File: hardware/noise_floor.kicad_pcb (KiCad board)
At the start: 2 copper layers, 51.5 x 61.6 mm, 13 parts, among them J1 Input, J2 Output, J3 DC Power, J4 IO/Effect Connector 1 (IO Sid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, J5 IO/Switch Connector 1 (IO Sid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, J6 IO/Switch Connector 2 (IO Sid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, J7 IO/Switch Connector 1 (Switch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, J8 IO/Switch Connector 2 (Switch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, SW1 Footswitch

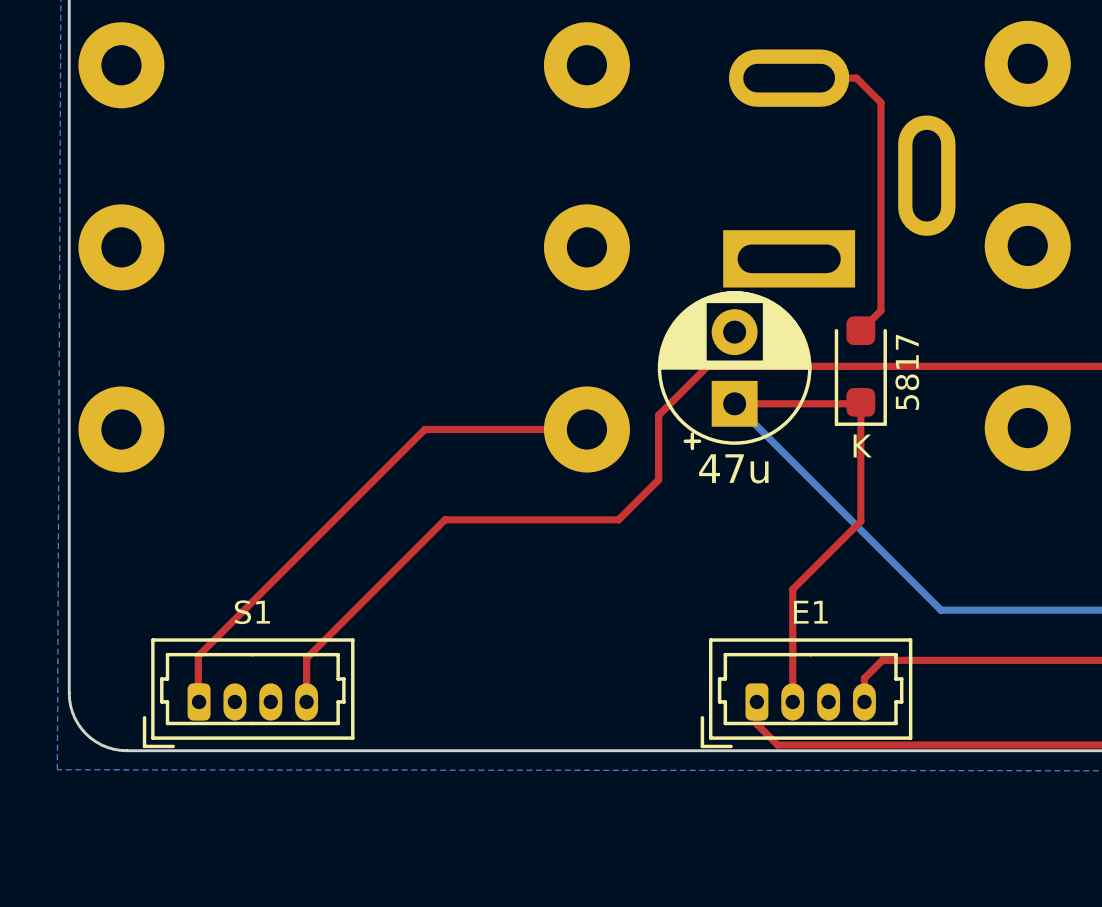
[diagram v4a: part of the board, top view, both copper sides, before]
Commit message: v0.05, added switched power input and optional battery connection
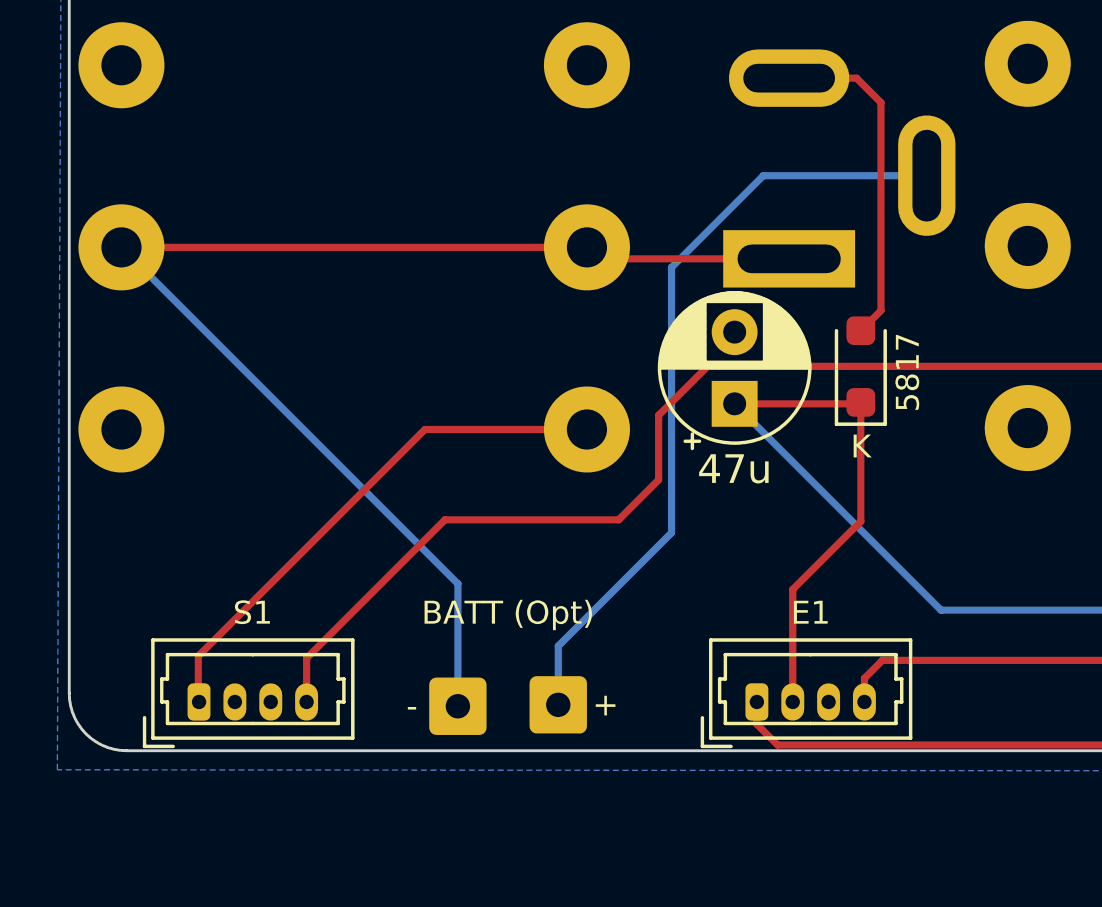
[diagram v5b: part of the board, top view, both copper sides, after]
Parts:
- added J4: Battery Negative (optional), Connector_Wire:SolderWire-0.25sqmm_1x01_D0.65mm_OD2mm, F.Cu at (29.1, 46.0)
- added J5: Battery Positive (optional), Connector_Wire:SolderWire-0.25sqmm_1x01_D0.65mm_OD2mm, F.Cu at (32.6, 45.9)
- renumbered J3 to J1, J8 to J10, J1 to J2, J2 to J3, J4 to J6, J5 to J7, J6 to J8, J7 to J9
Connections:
- J1 pad 1: GND -> /BATTERY_NEG
- J1 pad 3: unconnected-(J3-Pad3) -> /BATTERY_POS
- J2 pad R: GND -> /BATTERY_NEG
- J2 pad RN: unconnected-(J1-PadRN) -> /BATTERY_NEG
- J2 pad SN: unconnected-(J1-PadSN) -> GND
- J2 pad TN: unconnected-(J1-PadTN) -> GND
- J3 pad RN: unconnected-(J2-PadRN) -> GND
- J3 pad SN: unconnected-(J2-PadSN) -> GND
- J3 pad TN: unconnected-(J2-PadTN) -> GND
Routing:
- net /BATTERY_NEG: track 0.00 -> 44.3 mm
- net /BATTERY_POS: track 0.00 -> 27.1 mm

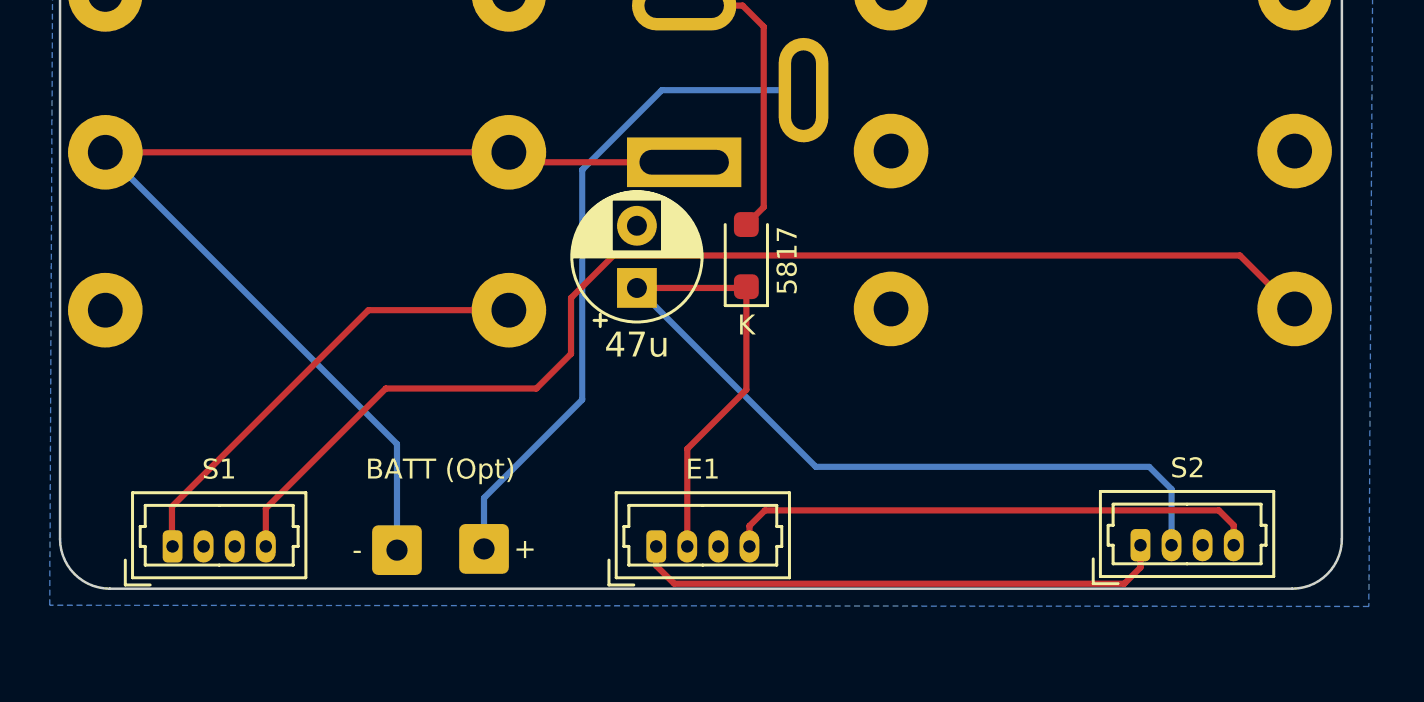
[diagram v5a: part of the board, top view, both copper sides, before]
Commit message: Remove ground from output switch line, fix ground split ground plane
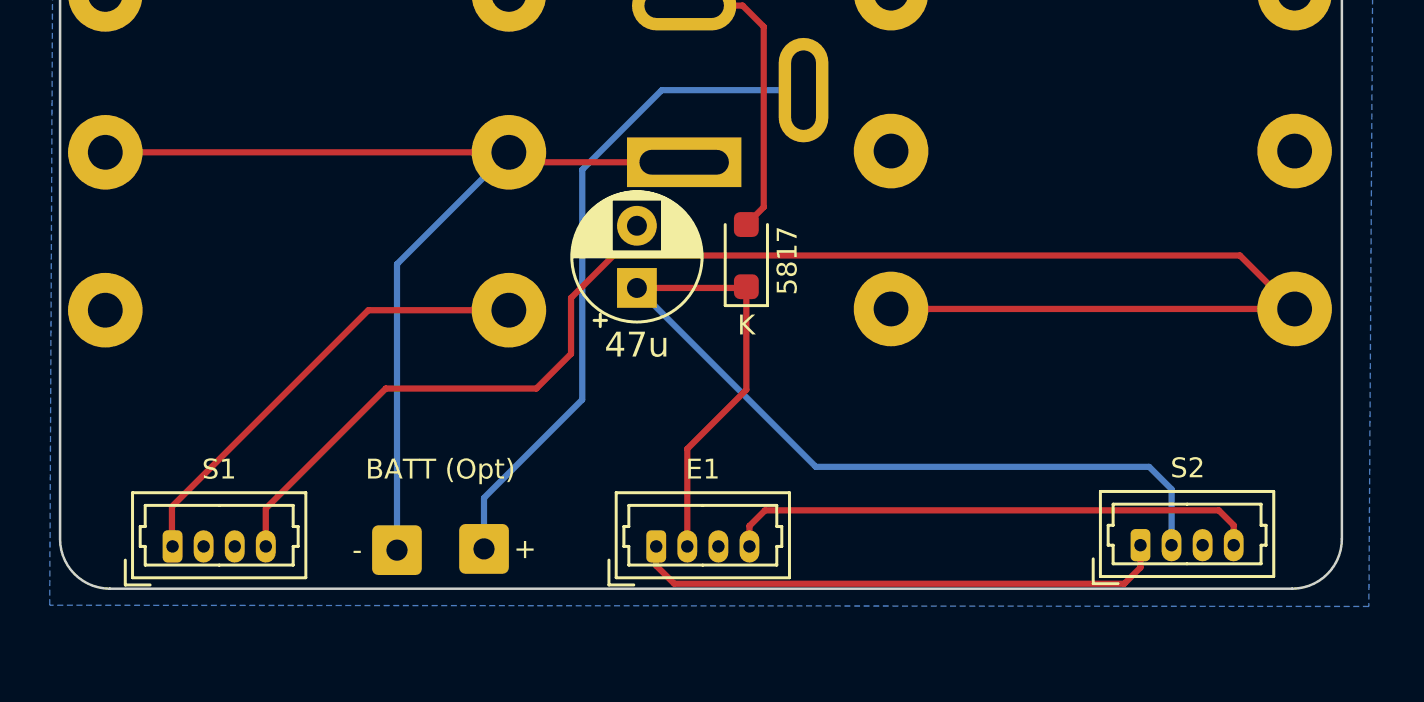
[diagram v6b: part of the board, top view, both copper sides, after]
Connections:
- J3 pad TN: GND -> /OUTPUT_TIP_IO
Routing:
- net /OUTPUT_TIP_IO: track 49.3 -> 65.6 mm
- net /BATTERY_NEG: track 44.3 -> 41.3 mm
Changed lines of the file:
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@@
     (title "Noise Floor Interface Boards")
     (date "2023-03-04")
-    (rev "v0.05")
+    (rev "v0.07")
     (comment 1 "github.com/whbeers/noise_floor")
   )
@@
       (net 4 "/OUTPUT_TIP_IO") (pintype "passive"))
     (pad "TN" thru_hole circle (at 0 -16.23 90) (size 3 3) (drill 1.4) (layers "*.Cu" "*.Mask")
-      (net 12 "GND") (pintype "passive"))
+      (net 4 "/OUTPUT_TIP_IO") (pintype "passive"))
     (model "${KICAD6_3DMODEL_DIR}/Connector_Audio.3dshapes/Jack_6.35mm_Neutrik_NMJ6HCD2_Horizontal.wrl"
       (offset (xyz 0 0 0))
@@
   (segment (start 27.95 36.3) (end 20.05 44.2) (width 0.25) (layer "F.Cu") (net 3))
   (segment (start 28.65 39.45) (end 34.705113 39.45) (width 0.25) (layer "F.Cu") (net 4))
+  (segment (start 65.2 36.25) (end 48.97 36.25) (width 0.25) (layer "F.Cu") (net 4))
   (segment (start 23.825 44.275) (end 28.65 39.45) (width 0.25) (layer "F.Cu") (net 4))
   (segment (start 37.805113 34.1) (end 63 34.1) (width 0.25) (layer "F.Cu") (net 4))
@@
   (segment (start 40.65 30.35) (end 34 30.35) (width 0.25) (layer "F.Cu") (net 14))
   (segment (start 34 30.35) (end 33.6 29.95) (width 0.25) (layer "F.Cu") (net 14))
-  (segment (start 17.37 29.95) (end 29.1 41.68) (width 0.25) (layer "B.Cu") (net 14))
-  (segment (start 29.1 41.68) (end 29.1 45.95) (width 0.25) (layer "B.Cu") (net 14))
+  (segment (start 33.6 29.95) (end 29.1 34.45) (width 0.25) (layer "B.Cu") (net 14))
+  (segment (start 29.1 34.45) (end 29.1 45.95) (width 0.25) (layer "B.Cu") (net 14))
   (segment (start 39.791 57.098) (end 39.791 60.423) (width 0.25) (layer "F.Cu") (net 15))
   (segment (start 36.55 30.65) (end 36.55 39.9) (width 0.25) (layer "B.Cu") (net 16))

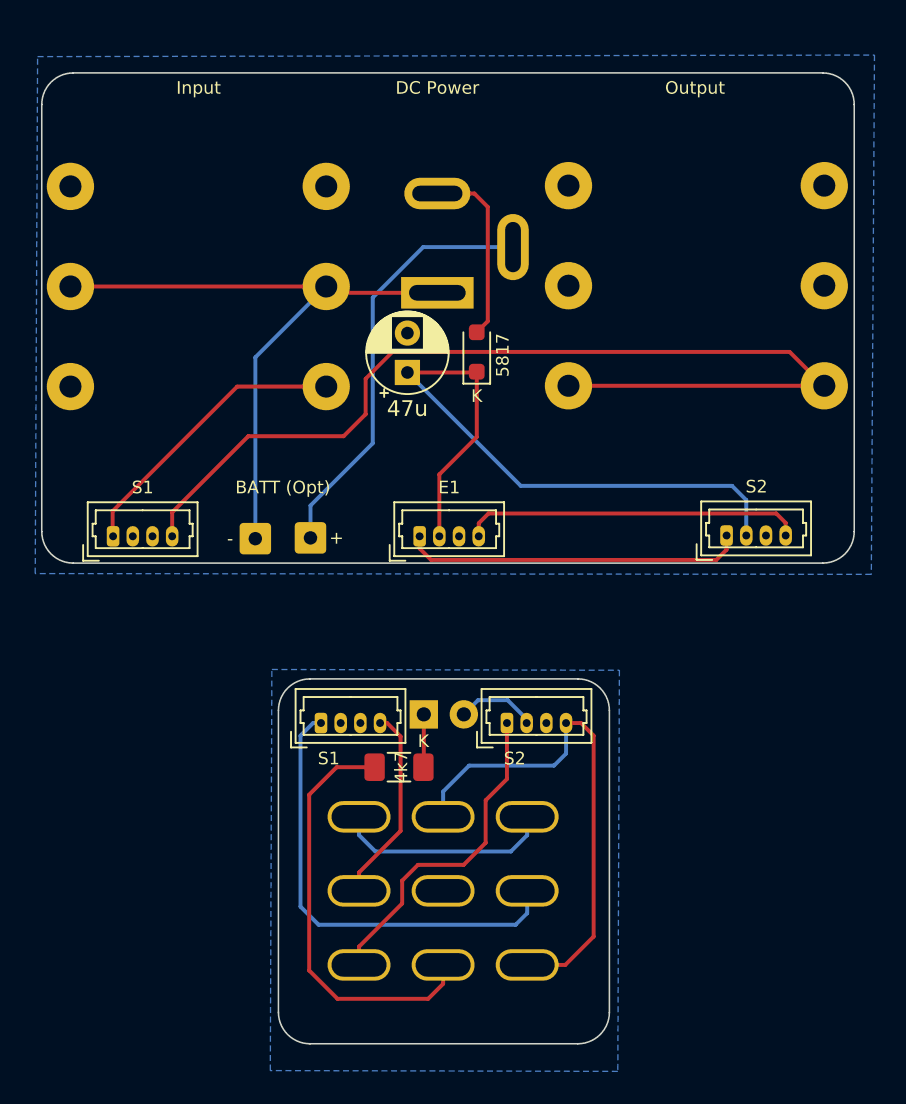
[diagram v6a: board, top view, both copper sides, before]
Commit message: slight adjustment to input switch behavior, add note about chassis ground
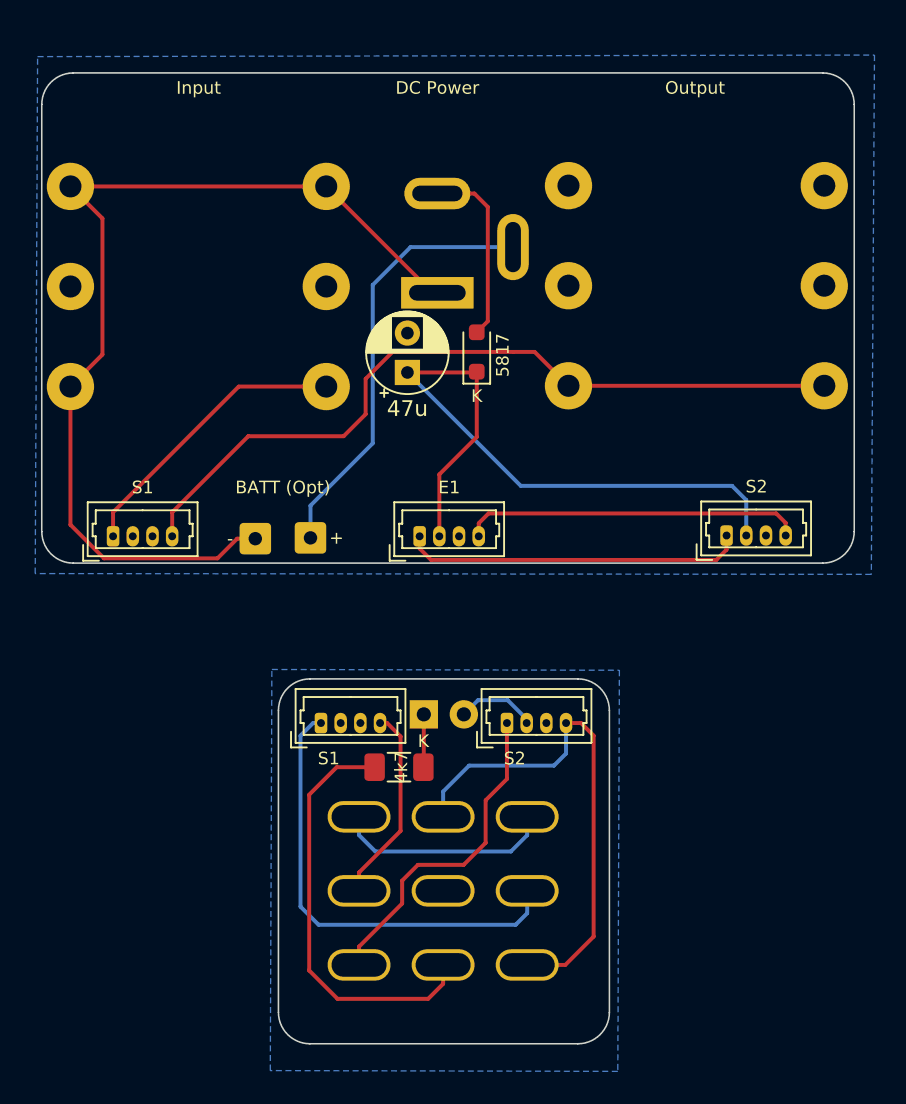
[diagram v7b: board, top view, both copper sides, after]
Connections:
- J2 pad R: /BATTERY_NEG -> GND
- J2 pad RN: /BATTERY_NEG -> GND
- J2 pad S: GND -> /BATTERY_NEG
- J2 pad SN: GND -> /BATTERY_NEG
- J2 pad TN: GND -> /BATTERY_NEG
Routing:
- net /BATTERY_NEG: track 41.3 -> 62.4 mm
- net /OUTPUT_TIP_IO: track 65.6 -> 49.3 mm
- net GND: track 0.00 -> 0.57 mm
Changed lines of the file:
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@@
       (stroke (width 0.1) (type solid)) (layer "B.Fab"))
     (pad "R" thru_hole circle (at 6.35 0 90) (size 3 3) (drill 1.4) (layers "*.Cu" "*.Mask")
+      (net 12 "GND") (pintype "passive"))
+    (pad "RN" thru_hole circle (at 6.35 -16.23 90) (size 3 3) (drill 1.4) (layers "*.Cu" "*.Mask")
+      (net 12 "GND") (pintype "passive"))
+    (pad "S" thru_hole circle (at 12.7 0 90) (size 3 3) (drill 1.4) (layers "*.Cu" "*.Mask")
       (net 14 "/BATTERY_NEG") (pintype "passive"))
-    (pad "RN" thru_hole circle (at 6.35 -16.23 90) (size 3 3) (drill 1.4) (layers "*.Cu" "*.Mask")
+    (pad "SN" thru_hole circle (at 12.7 -16.23 90) (size 3 3) (drill 1.4) (layers "*.Cu" "*.Mask")
       (net 14 "/BATTERY_NEG") (pintype "passive"))
-    (pad "S" thru_hole circle (at 12.7 0 90) (size 3 3) (drill 1.4) (layers "*.Cu" "*.Mask")
-      (net 12 "GND") (pintype "passive"))
-    (pad "SN" thru_hole circle (at 12.7 -16.23 90) (size 3 3) (drill 1.4) (layers "*.Cu" "*.Mask")
-      (net 12 "GND") (pintype "passive"))
     (pad "T" thru_hole circle (at 0 0 90) (size 3 3) (drill 1.4) (layers "*.Cu" "*.Mask")
       (net 3 "/INPUT_TIP_IO") (pintype "passive"))
     (pad "TN" thru_hole circle (at 0 -16.23 90) (size 3 3) (drill 1.4) (layers "*.Cu" "*.Mask")
-      (net 12 "GND") (pintype "passive"))
+      (net 14 "/BATTERY_NEG") (pintype "passive"))
     (model "${KICAD6_3DMODEL_DIR}/Connector_Audio.3dshapes/Jack_6.35mm_Neutrik_NMJ6HCD2_Horizontal.wrl"
       (offset (xyz 0 0 0))
@@
     (effects (font (size 0.8 0.8) (thickness 0.15)) (justify left bottom mirror))
   )
+  (gr_text_box "For enclosure ground (when necessary, such as with plastic audio jacks), solder a wire from GND_SW lug to footswitch washer."
+    (start 52.55 65.95) (end 69.5 69.7) (layer "Dwgs.User")
+      (effects (font (size 0.5 0.5) (thickness 0.125)) (justify left top))
+    (stroke (width 0.15) (type solid))  )
   (segment (start 43.85 32.155113) (end 43.15 32.855113) (width 0.25) (layer "F.Cu") (net 1))
   (segment (start 43.85 24.9) (end 43.85 32.155113) (width 0.25) (layer "F.Cu") (net 1))
@@
   (segment (start 35.682 64.764) (end 35.682 63.598) (width 0.25) (layer "B.Cu") (net 2))
   (segment (start 45.316 65.798) (end 36.716 65.798) (width 0.25) (layer "B.Cu") (net 2))
-  (segment (start 20.05 44.2) (end 20.05 45.775) (width 0.25) (layer "F.Cu") (net 3))
-  (segment (start 33.6 36.3) (end 27.95 36.3) (width 0.25) (layer "F.Cu") (net 3))
-  (segment (start 27.95 36.3) (end 20.05 44.2) (width 0.25) (layer "F.Cu") (net 3))
+  (segment (start 33.6 36.3) (end 28.05 36.3) (width 0.25) (layer "F.Cu") (net 3))
+  (segment (start 20.075 44.275) (end 20.075 45.8) (width 0.25) (layer "F.Cu") (net 3))
+  (segment (start 28.05 36.3) (end 20.075 44.275) (width 0.25) (layer "F.Cu") (net 3))
   (segment (start 28.65 39.45) (end 34.705113 39.45) (width 0.25) (layer "F.Cu") (net 4))
+  (segment (start 46.82 34.1) (end 45.5 34.1) (width 0.25) (layer "F.Cu") (net 4))
   (segment (start 65.2 36.25) (end 48.97 36.25) (width 0.25) (layer "F.Cu") (net 4))
   (segment (start 23.825 44.275) (end 28.65 39.45) (width 0.25) (layer "F.Cu") (net 4))
-  (segment (start 37.805113 34.1) (end 63 34.1) (width 0.25) (layer "F.Cu") (net 4))
   (segment (start 36.1 35.805113) (end 37.805113 34.1) (width 0.25) (layer "F.Cu") (net 4))
+  (segment (start 48.97 36.25) (end 46.82 34.1) (width 0.25) (layer "F.Cu") (net 4))
+  (segment (start 37.805113 34.1) (end 45.5 34.1) (width 0.25) (layer "F.Cu") (net 4))
   (segment (start 34.705113 39.45) (end 36.1 38.055113) (width 0.25) (layer "F.Cu") (net 4))
-  (segment (start 63 34.1) (end 65.2 36.3) (width 0.25) (layer "F.Cu") (net 4))
   (segment (start 23.825 45.8) (end 23.825 44.275) (width 0.25) (layer "F.Cu") (net 4))
   (segment (start 36.1 38.055113) (end 36.1 35.805113) (width 0.25) (layer "F.Cu") (net 4))
@@
   (segment (start 48.816 59.584) (end 48.052 60.348) (width 0.25) (layer "B.Cu") (net 10))
   (segment (start 42.666 60.348) (end 41.016 61.998) (width 0.25) (layer "B.Cu") (net 10))
+  (segment (start 34 30.35) (end 33.6 29.95) (width 0.25) (layer "F.Cu") (net 12))
   (segment (start 39.416 66.648) (end 38.416 67.648) (width 0.25) (layer "F.Cu") (net 13))
   (segment (start 43.716 62.548) (end 43.716 65.248) (width 0.25) (layer "F.Cu") (net 13))
@@
   (segment (start 35.682 71.832) (end 35.682 72.996) (width 0.25) (layer "F.Cu") (net 13))
   (segment (start 38.416 69.098) (end 35.682 71.832) (width 0.25) (layer "F.Cu") (net 13))
-  (segment (start 33.6 29.95) (end 17.37 29.95) (width 0.25) (layer "F.Cu") (net 14))
-  (segment (start 40.65 30.35) (end 34 30.35) (width 0.25) (layer "F.Cu") (net 14))
-  (segment (start 34 30.35) (end 33.6 29.95) (width 0.25) (layer "F.Cu") (net 14))
-  (segment (start 33.6 29.95) (end 29.1 34.45) (width 0.25) (layer "B.Cu") (net 14))
-  (segment (start 29.1 34.45) (end 29.1 45.95) (width 0.25) (layer "B.Cu") (net 14))
+  (segment (start 29.1 45.95) (end 27.95 45.95) (width 0.25) (layer "F.Cu") (net 14))
+  (segment (start 26.7 47.2) (end 19.5 47.2) (width 0.25) (layer "F.Cu") (net 14))
+  (segment (start 19.5 47.2) (end 17.37 45.07) (width 0.25) (layer "F.Cu") (net 14))
+  (segment (start 40.65 30.35) (end 40.35 30.35) (width 0.25) (layer "F.Cu") (net 14))
+  (segment (start 33.6 23.6) (end 17.37 23.6) (width 0.25) (layer "F.Cu") (net 14))
+  (segment (start 40.35 30.35) (end 33.6 23.6) (width 0.25) (layer "F.Cu") (net 14))
+  (segment (start 17.37 23.6) (end 19.4 25.63) (width 0.25) (layer "F.Cu") (net 14))
+  (segment (start 27.95 45.95) (end 26.7 47.2) (width 0.25) (layer "F.Cu") (net 14))
+  (segment (start 17.37 45.07) (end 17.37 36.3) (width 0.25) (layer "F.Cu") (net 14))
+  (segment (start 19.4 25.63) (end 19.4 34.27) (width 0.25) (layer "F.Cu") (net 14))
+  (segment (start 19.4 34.27) (end 17.37 36.3) (width 0.25) (layer "F.Cu") (net 14))
   (segment (start 39.791 57.098) (end 39.791 60.423) (width 0.25) (layer "F.Cu") (net 15))
-  (segment (start 36.55 30.65) (end 36.55 39.9) (width 0.25) (layer "B.Cu") (net 16))
+  (segment (start 32.6 43.85) (end 32.6 45.9) (width 0.25) (layer "B.Cu") (net 16))
+  (segment (start 36.55 29.85) (end 36.55 39.9) (width 0.25) (layer "B.Cu") (net 16))
+  (segment (start 38.95 27.45) (end 36.55 29.85) (width 0.25) (layer "B.Cu") (net 16))
+  (segment (start 45.45 27.45) (end 38.95 27.45) (width 0.25) (layer "B.Cu") (net 16))
   (segment (start 36.55 39.9) (end 32.6 43.85) (width 0.25) (layer "B.Cu") (net 16))
-  (segment (start 32.6 43.85) (end 32.6 45.9) (width 0.25) (layer "B.Cu") (net 16))
-  (segment (start 39.75 27.45) (end 36.55 30.65) (width 0.25) (layer "B.Cu") (net 16))
-  (segment (start 45.45 27.45) (end 39.75 27.45) (width 0.25) (layer "B.Cu") (net 16))
   (segment (start 46.316 57.398) (end 45.116 56.198) (width 0.25) (layer "B.Cu") (net 17))
   (segment (start 43.231 56.198) (end 42.331 57.098) (width 0.25) (layer "B.Cu") (net 17))
